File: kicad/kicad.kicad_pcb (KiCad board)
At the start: 2 copper layers, 458 x 143.5 mm, 256 parts, among them J1 USB_B_Micro, J2 SWD, J3 pwr_led+, J4 pwr_led-, J5 caps_led+, J6 caps_led-, U1 AMS1117-3.3, Y1 16MGz, sw1 Esc, sw10 Z, sw100 N5, sw101 N6, sw102 N2, sw103 N1, sw104 N0, sw105 MPlay, sw106 MFwd, sw107 NSlash, sw108 NStar, sw109 N8, sw11 LCtrl, sw110 N9, sw111 NMinus, sw112 NPlus, sw113 NEnter, sw114 N3, sw115 NPeriod, sw12 LSys, sw13 F2, sw14 F3, sw15 2, sw16 3, sw17 W, sw18 E, sw19 S, sw2 F1, sw20 D, sw21 X, sw22 C, sw23 LAlt, sw24 THome, sw25 F4, sw26 F5, sw27 4, sw28 5, sw29 R, sw3 Tilda, sw30 T, sw31 F, sw32 G, sw33 V, sw34 B, sw35 LSpace, sw36 TLeft, sw37 F6, sw38 F7, sw39 6, sw4 1, sw40 7, sw41 Y, sw42 U, sw43 H, sw44 J, sw45 N, sw46 M, sw47 TUp, sw48 TDown, sw49 F8, sw5 Tab, sw50 F9, sw51 8, sw52 9, sw53 I, sw54 O, sw55 K, sw56 L, sw57 Comma, sw58 Period, sw59 RSpace, sw6 Q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

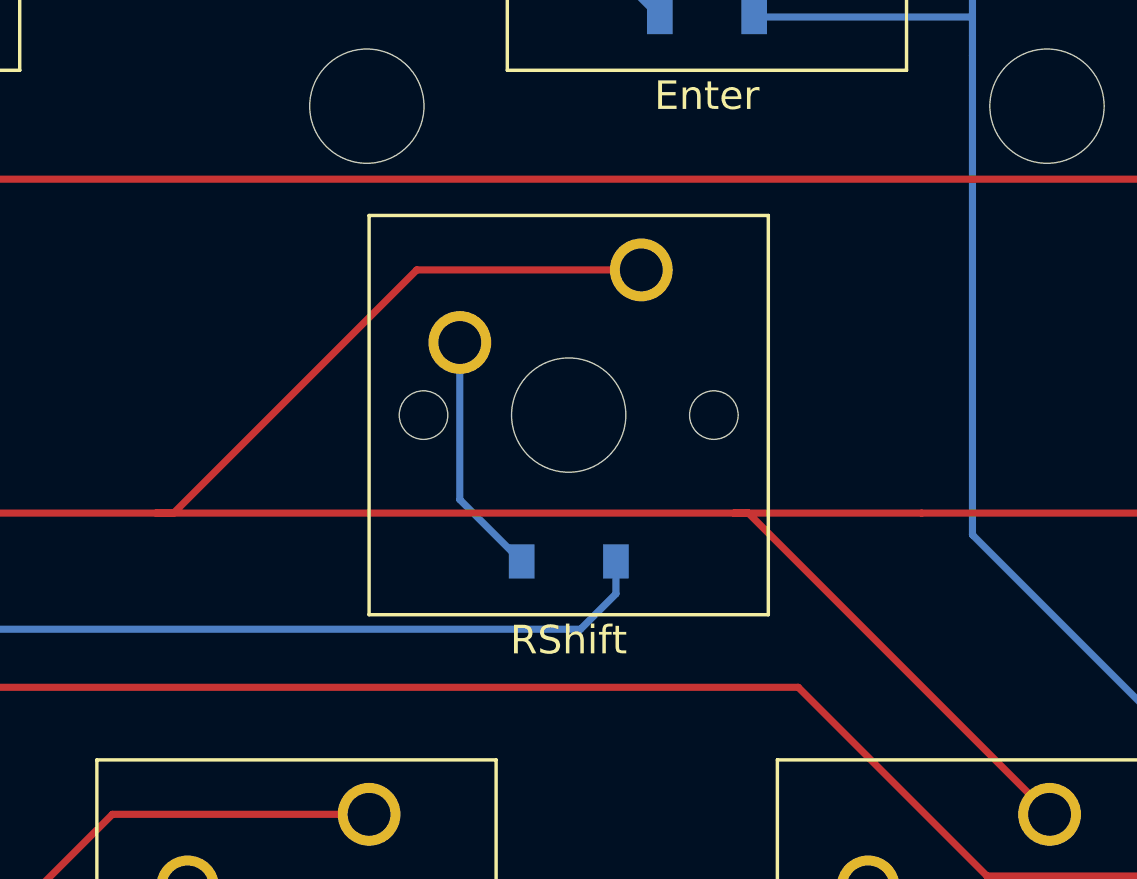
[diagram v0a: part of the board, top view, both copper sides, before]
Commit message: correct RShift footprint
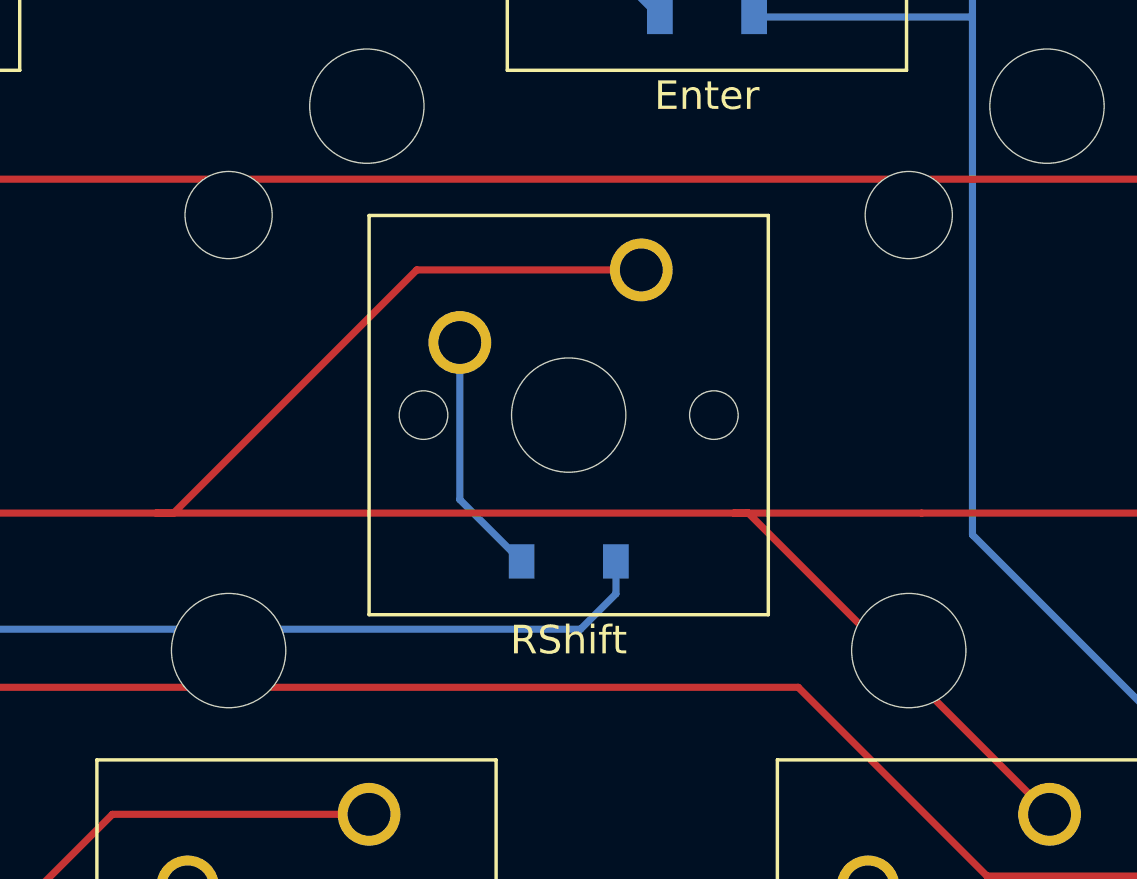
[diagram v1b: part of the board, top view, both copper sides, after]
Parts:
- sw70: footprint Button_Switch_Keyboard:SW_Cherry_MX_1.00u_PCB -> Button_Switch_Keyboard:SW_Cherry_MX_2.75u_PCB
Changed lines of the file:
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@@
     )
   )
-  (footprint "Button_Switch_Keyboard:SW_Cherry_MX_1.00u_PCB" (layer "F.Cu")
+  (footprint "Button_Switch_Keyboard:SW_Cherry_MX_2.75u_PCB" (layer "F.Cu")
     (at 350.1565 181.7)
-    (descr "Cherry MX keyswitch, 1.00u, PCB mount, http://cherryamericas.com/wp-content/uploads/2014/12/mx_cat.pdf")
-    (tags "Cherry MX keyswitch 1.00u PCB")
+    (descr "Cherry MX keyswitch, 2.75u, PCB mount, http://cherryamericas.com/wp-content/uploads/2014/12/mx_cat.pdf")
+    (tags "Cherry MX keyswitch 2.75u PCB")
     (property "Sheetfile" "kicad.kicad_sch")
     (property "Sheetname" "")
     (attr through_hole)
-    (fp_text reference "sw70" (at -2.54 -2.794) (layer "F.Fab") hide
+    (fp_text reference "sw70" (at -2.54 -2.794) (layer "F.SilkS") hide
       (effects (font (size 1 1) (thickness 0.15)))
     )
@@
       (effects (font (size 1 1) (thickness 0.15)))
     )
-    (fp_line (start -9.525 -1.905) (end 4.445 -1.905) (layer "F.SilkS") (width 0.12))
     (fp_line (start 4.445 -1.905) (end 4.445 12.065) (layer "F.SilkS") (width 0.12))
     (fp_line (start 4.445 12.065) (end -9.525 12.065) (layer "F.SilkS") (width 0.12))
     (fp_line (start -9.525 12.065) (end -9.525 -1.905) (layer "F.SilkS") (width 0.12))
-    (fp_line (start 6.985 14.605) (end -12.065 14.605) (layer "Dwgs.User") (width 0.15))
-    (fp_line (start -12.065 14.605) (end -12.065 -4.445) (layer "Dwgs.User") (width 0.15))
-    (fp_line (start 6.985 -4.445) (end 6.985 14.605) (layer "Dwgs.User") (width 0.15))
-    (fp_line (start -12.065 -4.445) (end 6.985 -4.445) (layer "Dwgs.User") (width 0.15))
+    (fp_line (start -9.525 -1.905) (end 4.445 -1.905) (layer "F.SilkS") (width 0.12))
+    (fp_line (start 23.65375 14.605) (end -28.73375 14.605) (layer "Dwgs.User") (width 0.15))
+    (fp_line (start -28.73375 -4.445) (end 23.65375 -4.445) (layer "Dwgs.User") (width 0.15))
+    (fp_line (start -28.73375 14.605) (end -28.73375 -4.445) (layer "Dwgs.User") (width 0.15))
+    (fp_line (start 23.65375 -4.445) (end 23.65375 14.605) (layer "Dwgs.User") (width 0.15))
+    (fp_line (start 4.06 11.68) (end -9.14 11.68) (layer "F.CrtYd") (width 0.05))
+    (fp_line (start -9.14 -1.52) (end 4.06 -1.52) (layer "F.CrtYd") (width 0.05))
+    (fp_line (start -9.14 11.68) (end -9.14 -1.52) (layer "F.CrtYd") (width 0.05))
     (fp_line (start 4.06 -1.52) (end 4.06 11.68) (layer "F.CrtYd") (width 0.05))
-    (fp_line (start -9.14 11.68) (end -9.14 -1.52) (layer "F.CrtYd") (width 0.05))
-    (fp_line (start -9.14 -1.52) (end 4.06 -1.52) (layer "F.CrtYd") (width 0.05))
-    (fp_line (start 4.06 11.68) (end -9.14 11.68) (layer "F.CrtYd") (width 0.05))
+    (fp_line (start -8.89 11.43) (end -8.89 -1.27) (layer "F.Fab") (width 0.1))
     (fp_line (start 3.81 11.43) (end -8.89 11.43) (layer "F.Fab") (width 0.1))
+    (fp_line (start -8.89 -1.27) (end 3.81 -1.27) (layer "F.Fab") (width 0.1))
     (fp_line (start 3.81 -1.27) (end 3.81 11.43) (layer "F.Fab") (width 0.1))
-    (fp_line (start -8.89 -1.27) (end 3.81 -1.27) (layer "F.Fab") (width 0.1))
-    (fp_line (start -8.89 11.43) (end -8.89 -1.27) (layer "F.Fab") (width 0.1))
     (pad "" np_thru_hole circle (at -7.62 5.08) (size 1.7 1.7) (drill 1.7) (layers *.Cu *.Mask))
+    (pad "" np_thru_hole circle (at 9.36 -1.92) (size 3.05 3.05) (drill 3.05) (layers *.Cu *.Mask))
+    (pad "" np_thru_hole circle (at -14.44 -1.92) (size 3.05 3.05) (drill 3.05) (layers *.Cu *.Mask))
     (pad "" np_thru_hole circle (at -2.54 5.08) (size 4 4) (drill 4) (layers *.Cu *.Mask))
     (pad "" np_thru_hole circle (at 2.54 5.08) (size 1.7 1.7) (drill 1.7) (layers *.Cu *.Mask))
+    (pad "" np_thru_hole circle (at 9.36 13.32) (size 4 4) (drill 4) (layers *.Cu *.Mask))
+    (pad "" np_thru_hole circle (at -14.44 13.32) (size 4 4) (drill 4) (layers *.Cu *.Mask))
     (pad "1" thru_hole circle (at 0 0) (size 2.2 2.2) (drill 1.5) (layers *.Cu *.Mask)
       (net 25 "ROW10") (pinfunction "1") (pintype "passive"))
     (pad "2" thru_hole circle (at -6.35 2.54) (size 2.2 2.2) (drill 1.5) (layers *.Cu *.Mask)
       (net 125 "Net-(D70-Pad2)") (pinfunction "2") (pintype "passive"))
-    (model "${KICAD6_3DMODEL_DIR}/Button_Switch_Keyboard.3dshapes/SW_Cherry_MX_1.00u_PCB.wrl"
+    (model "${KICAD6_3DMODEL_DIR}/Button_Switch_Keyboard.3dshapes/SW_Cherry_MX_2.75u_PCB.wrl"
       (offset (xyz 0 0 0))
       (scale (xyz 1 1 1))

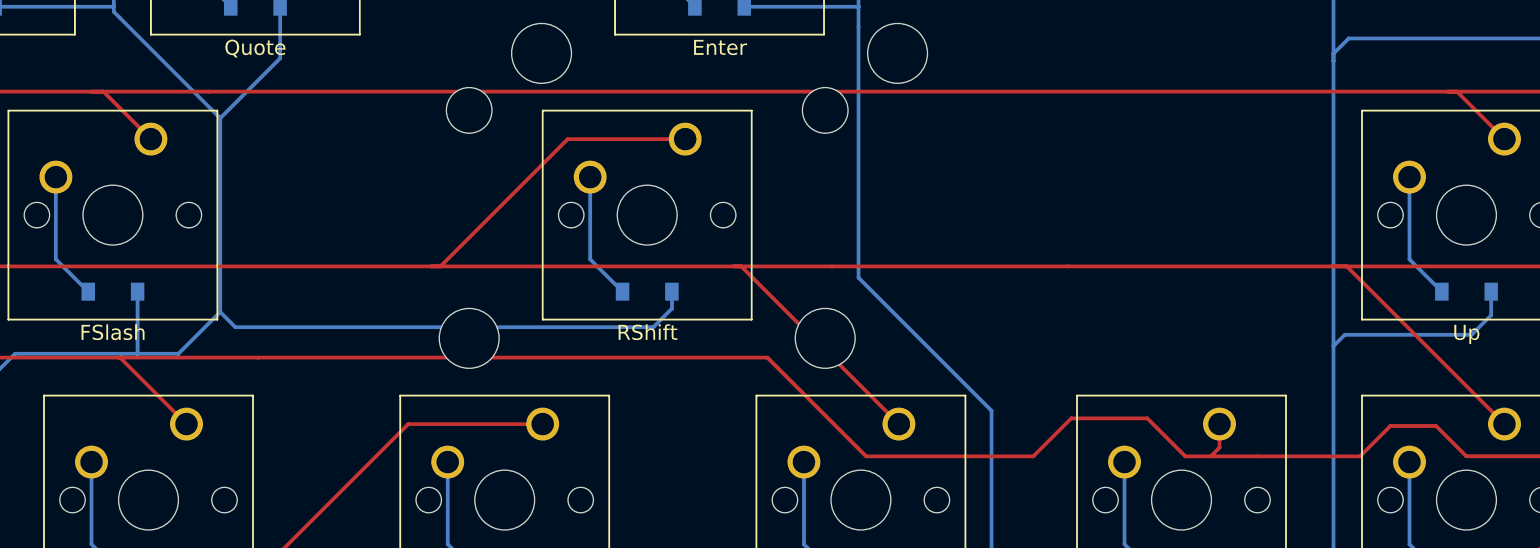
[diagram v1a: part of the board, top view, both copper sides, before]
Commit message: fix traces getting clobbered by new holes
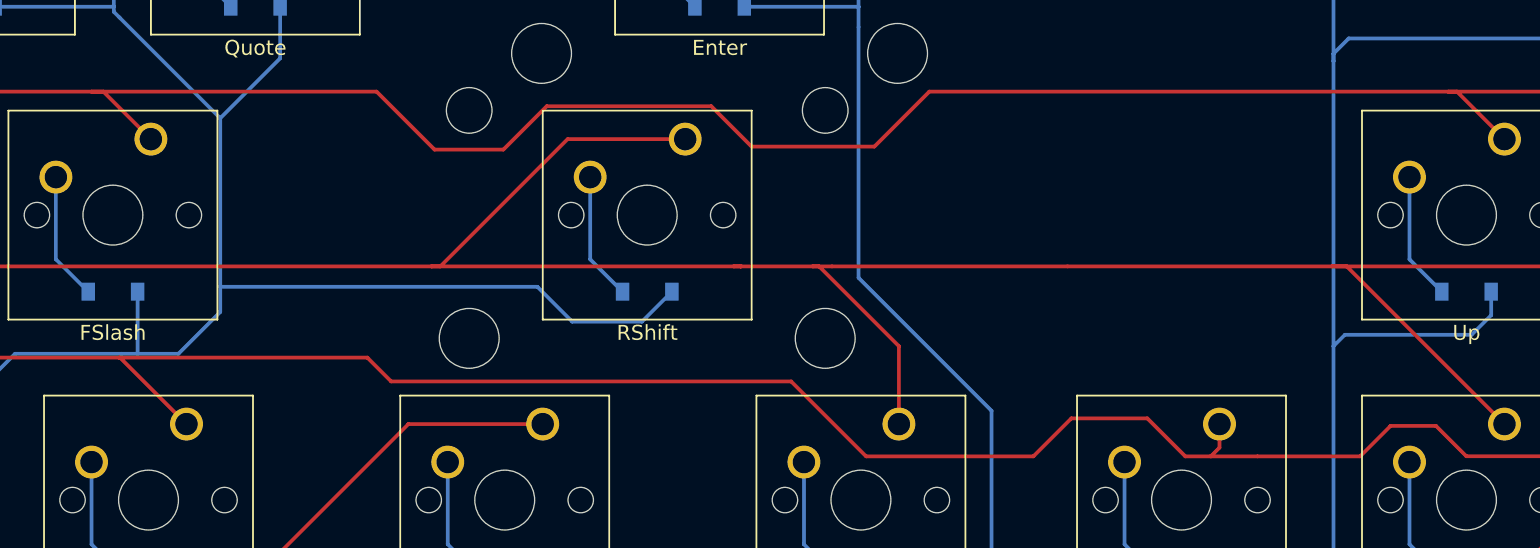
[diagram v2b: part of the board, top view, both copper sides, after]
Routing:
- net ROW9: track 529.6 -> 535.1 mm
- net ROW10: track 624.4 -> 622.7 mm

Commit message: fix DRC warnings from moving to kicad 7
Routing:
- net ROW5: track 442.4 -> 447.2 mm

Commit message: move diodes
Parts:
- D1, D10, D100, D101, D102, D103, D104, D105, D106, D107, D108, D109, D11, D110, D111, D112, D113, D114, D115, D12, D13, D14, D15, D16, D17, D18, D19, D2, D20, D21, D22, D23, D24, D25, D26, D27, D28, D29, D3, D30, D31, D32, D33, D34, D35, D36, D37, D38, D39, D4, D40, D41, D42, D43, D44, D45, D46, D47, D48, D49, D5, D50, D51, D52, D53, D54, D55, D56, D57, D58, D59, D6, D60, D61, D62, D63, D64, D65, D66, D67, D68, D69, D7, D70, D71, D72, D73, D74, D75, D76, D77, D78, D79, D8, D80, D81, D82, D83, D84, D85, D86, D87, D88, D89, D9, D90, D91, D92, D93, D94, D95, D96, D97, D98, D99: moved to F.Cu
- moved D33 7.33 mm to (204.0, 195.5)
- moved D62 6.65 mm to (350.0, 120.3)
- moved D73 6.19 mm to (360.5, 120.6)
- moved D102 5.97 mm to (455.5, 196.2)
- moved D103 5.80 mm to (444.0, 196.5)
- moved D22 5.16 mm to (180.9, 196.5)
- moved D24 4.86 mm to (183.3, 234.9)
- moved D36 4.86 mm to (202.4, 234.9)
- moved D48 4.86 mm to (221.4, 234.9)
- moved D60 4.86 mm to (240.5, 234.9)
- moved D72 4.86 mm to (259.5, 234.9)
- moved D112 4.73 mm to (497.6, 168.1)
- moved D113 4.73 mm to (497.6, 206.2)
- moved D115 4.60 mm to (478.7, 215.6)
- moved D92 4.60 mm to (383.5, 215.6)
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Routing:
- net COLUMN7: track 422.1 -> 390.0 mm
- net COLUMN5: track 549.1 -> 518.0 mm
- net COLUMN3: track 606.0 -> 579.2 mm
- net COLUMN6: track 471.1 -> 445.6 mm
- net COLUMN4: track 541.3 -> 515.9 mm
- net COLUMN8: track 388.8 -> 366.0 mm
- net COLUMN2: track 601.7 -> 583.3 mm
- net COLUMN9: track 355.4 -> 337.4 mm
- net COLUMN10: track 330.4 -> 323.5 mm
- net Net-(D62-A): track 8.56 -> 15.1 mm
- net Net-(D33-A): track 8.67 -> 14.8 mm
- net Net-(D103-A): track 8.56 -> 14.6 mm
- net Net-(D22-A): track 8.56 -> 14.1 mm
- net Net-(D72-A): track 8.56 -> 13.4 mm
- net Net-(D60-A): track 8.56 -> 13.4 mm
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
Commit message: add vias, passing DRC. PCB now 1-sided yay
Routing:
- net ROW4: track 594.9 -> 592.4 mm, vias 0 -> 1
- net COLUMN8: track 366.0 -> 368.3 mm, vias 1 -> 2
- net COLUMN9: track 337.4 -> 339.4 mm, vias 1 -> 2
- net ROW6: track 595.1 -> 597.0 mm, vias 0 -> 1
- net ROW7: track 533.6 -> 535.3 mm, vias 0 -> 1
- net ROW5: track 447.2 -> 448.7 mm, vias 0 -> 1
- net ROW8: track 618.4 -> 619.9 mm, vias 0 -> 1
- net COLUMN7: track 390.0 -> 391.3 mm, vias 1 -> 2
- net COLUMN10: track 323.5 -> 322.3 mm, vias 1 -> 0
- net ROW9: track 535.1 -> 536.3 mm, vias 0 -> 1
- net COLUMN6: track 445.6 -> 446.5 mm, vias 1 -> 2
- net COLUMN1: track 638.8 -> 638.2 mm, vias 1 -> 2
- net COLUMN5: track 518.0 -> 518.4 mm, vias 1 -> 2
- net COLUMN4: track 515.9 -> 516.3 mm, vias 1 -> 2
- net ROW12: track 585.2 -> 585.5 mm, vias 0 -> 1
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
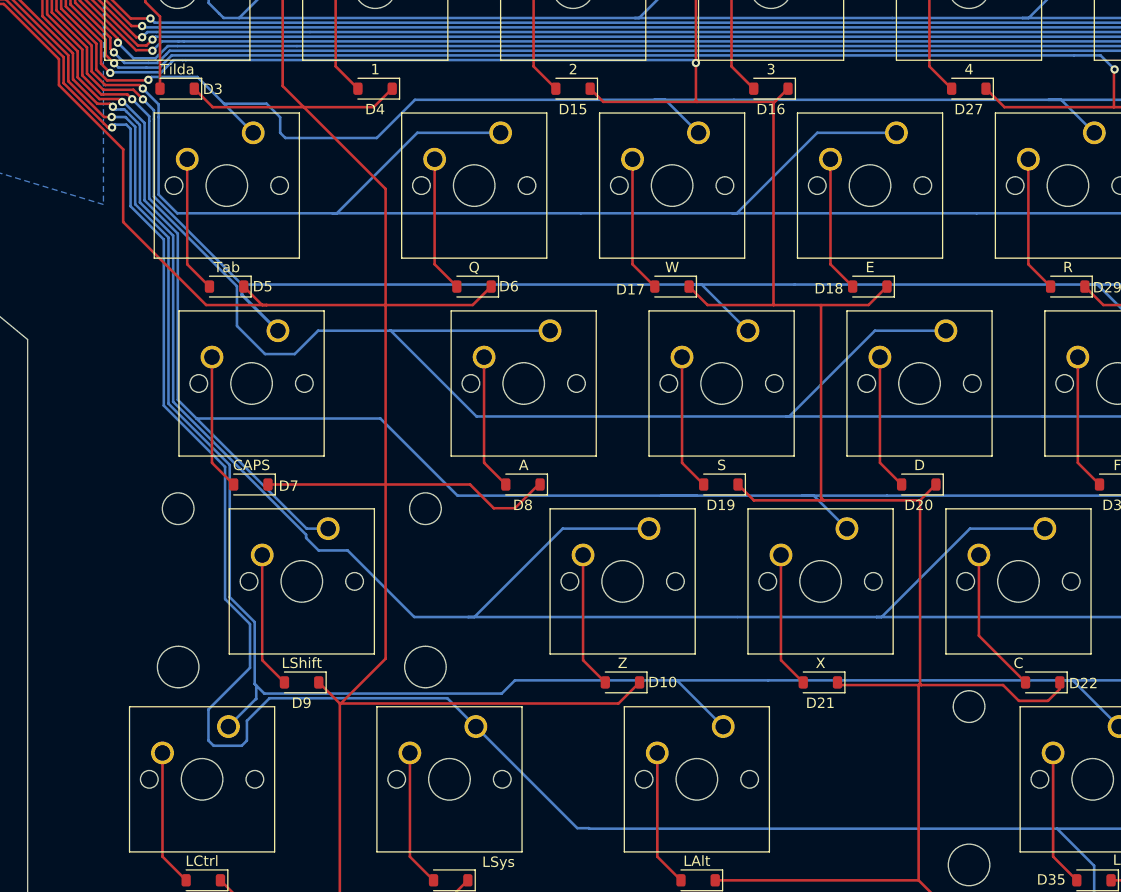
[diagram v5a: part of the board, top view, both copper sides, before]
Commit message: Some touch ups and fix the 3d model for the connector
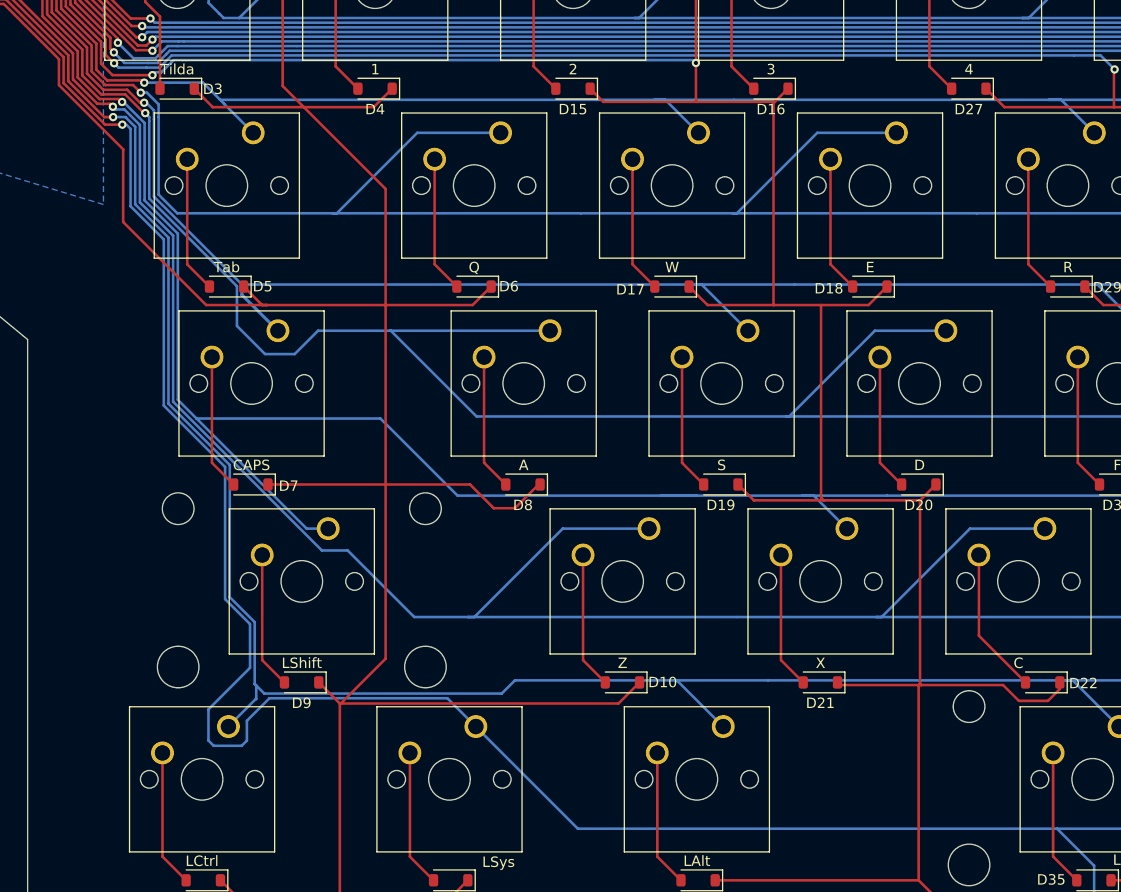
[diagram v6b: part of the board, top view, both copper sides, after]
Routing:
- net ROW5: track 448.7 -> 445.1 mm

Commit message: square board
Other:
- board size 458 x 143.5 mm -> 458 x 144 mm
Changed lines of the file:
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@@
   )
   (footprint "Connector_USB:USB_Micro-B_Wuerth_629105150521" (layer "F.Cu")
-    (at 71.375 99.955 180)
+    (at 71.375 100 180)
     (descr "USB Micro-B receptacle, http://www.mouser.com/ds/2/445/629105150521-469306.pdf")
     (tags "usb micro receptacle")
@@
     )
   )
-  (gr_poly
-    (pts
-      (xy 512.175 96)
-      (xy 512.175 220.5)
-      (xy 274.175 220.5)
-      (xy 274.175 239.5)
-      (xy 168.675 239.5)
-      (xy 168.675 220)
-      (xy 83.175 220)
-      (xy 83.175 163.5)
-      (xy 54.175 139.5)
-      (xy 54.175 96)
-    )
-    (stroke (width 0.1) (type solid)) (fill none) (layer "Edge.Cuts"))
+  (gr_rect (start 54 96) (end 512 240)
+    (stroke (width 0.15) (type default)) (fill none) (layer "Edge.Cuts"))
   (segment (start 93.775 118.161) (end 95.916 120.302) (width 0.25) (layer "F.Cu") (net 1))
   (segment (start 93.775 108.04) (end 93.775 118.161) (width 0.25) (layer "F.Cu") (net 1))
@@
   (segment (start 72.965 130.415) (end 72.965 131.525) (width 0.25) (layer "F.Cu") (net 171))
   (segment (start 72.475 129.925) (end 72.965 130.415) (width 0.25) (layer "F.Cu") (net 171))
-  (zone (net 12) (net_name "GND") (layer "B.Cu") (hatch edge 0.508)
+  (zone (net 12) (net_name "GND") (layer "B.Cu") (hatch edge 0.5)
     (connect_pads (clearance 0.508))
-    (min_thickness 0.254) (filled_areas_thickness no)
-    (fill yes (thermal_gap 0.508) (thermal_bridge_width 0.508))
+    (min_thickness 0.25) (filled_areas_thickness no)
+    (fill yes (thermal_gap 0.5) (thermal_bridge_width 0.5) (island_removal_mode 1) (island_area_min 10))
     (polygon
       (pts
-        (xy 90.475 150.5)
-        (xy 54.175 139.5)
-        (xy 54.175 96.05)
-        (xy 90.45 96.05)
+        (xy 54 96)
+        (xy 88 96)
+        (xy 88 139)
+        (xy 54 139)
       )
     )
